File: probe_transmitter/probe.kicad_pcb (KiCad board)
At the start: 2 copper layers, 28.5 x 28.5 mm, 22 parts, among them J2 Conn_01x06, Q1 PMST2222, Q2 PMST2222, U2 ATtiny84-20M

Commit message: -add fix connector
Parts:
- added +1: PB0, TestPoint:TestPoint_Pad_D1.0mm, B.Cu at (109.6, 109.0)
- added -1: PB0, TestPoint:TestPoint_Pad_D1.0mm, B.Cu at (107.9, 110.6)
- R1: value R39 -> R1K
- R2: value R39 -> R1k
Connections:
- J2 pad 1: +3.3V -> GND
- J2 pad 6: GND -> +3.3V
- Q1 pad 3: Net-(J2-Pin_2) -> Net-(J2-Pin_5)
- Q2 pad 3: Net-(J2-Pin_3) -> Net-(J2-Pin_4)
- R5 pad 1: Net-(J2-Pin_2) -> Net-(J2-Pin_5)
- U2 pad 15: Net-(J2-Pin_5) -> Net-(J2-Pin_2)
- U2 pad 3: Net-(J2-Pin_4) -> Net-(J2-Pin_3)
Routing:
- net +3.3V: track 31.4 -> 61.0 mm
- net GND: track 28.8 -> 46.5 mm, vias 2 -> 1
- net Net-(J2-Pin_2): track 19.4 -> 36.3 mm, vias 1 -> 3
- net Net-(J2-Pin_4): track 19.5 -> 31.8 mm
- net Net-(J2-Pin_3): track 29.9 -> 20.3 mm
- net Net-(J2-Pin_5): track 24.5 -> 21.4 mm
- net /PAD1: track 69.8 -> 69.3 mm
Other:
- board text added: "G"

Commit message: -add to production
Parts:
- removed +1, -1, MOSI1: PB0, TestPoint:TestPoint_Pad_D1.0mm
- removed the ? at (111.3, 98.1)
- removed the ? at (111.3, 101.9)
- removed MISO1: PB1, TestPoint:TestPoint_Pad_D1.0mm
- removed RES1: PB5, TestPoint:TestPoint_Pad_D1.0mm
- removed SCL1: PB2, TestPoint:TestPoint_Pad_D1.0mm
- added +: PB0, TestPoint:TestPoint_Pad_D1.0mm, B.Cu at (105.1, 98.7)
- added -: PB0, TestPoint:TestPoint_Pad_D1.0mm, B.Cu at (104.7, 101.5)
- added ?: , , F.Cu at (110.3, 97.5)
- added ?: , , F.Cu at (110.3, 101.3)
- added MISO: PB1, TestPoint:TestPoint_Pad_D1.0mm, F.Cu at (106.9, 110.0)
- added MOSI: PB0, TestPoint:TestPoint_Pad_D1.0mm, F.Cu at (104.9, 111.2)
- added RES: PB5, TestPoint:TestPoint_Pad_D1.0mm, F.Cu at (102.8, 112.1)
- added SCL: PB2, TestPoint:TestPoint_Pad_D1.0mm, F.Cu at (108.6, 108.4)
-  : value Touch Probe v1.4 -> Touch Probe v1.5
- moved D4 1.61 mm to (99.0, 91.9)
- moved   1.17 mm to (90.0, 99.3)
- moved 1 1.17 mm to (91.7, 90.6)
- moved 2 1.17 mm to (94.9, 88.7)
- moved 3 1.17 mm to (95.0, 110.2)
- moved D5 1.17 mm to (98.9, 106.3)
- moved J2 1.17 mm to (102.8, 93.0)
- moved Q1 1.17 mm to (87.4, 97.4)
- moved Q2 1.17 mm to (87.4, 100.9)
- moved R1 1.17 mm to (90.1, 97.4)
- moved R2 1.17 mm to (90.1, 100.9)
- moved R5 1.17 mm to (91.7, 97.4)
- moved R6 1.17 mm to (91.7, 100.9)
- moved R7 1.17 mm to (92.3, 104.2)
- moved U2 1.17 mm to (103.8, 106.1)
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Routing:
- net +3.3V: track 61.0 -> 15.8 mm
- net Net-(J2-Pin_3): track 20.3 -> 21.5 mm
- net Net-(J2-Pin_5): track 21.4 -> 20.2 mm
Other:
- board text added: "+"
- board text added: "-"
- board text added: "LOW"
- board text added: "TOCH"
- board text removed: "G"

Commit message: -change hole ball 3.25/2.5
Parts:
-  : value Touch Probe v1.5 -> Touch Probe v1.6
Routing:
- net GND: track 46.3 -> 47.0 mm
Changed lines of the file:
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@@
 		(pad "1" thru_hole circle
 			(at 0 0)
-			(size 2.5 2.5)
-			(drill 1.6)
+			(size 3.25 3.25)
+			(drill 2.5)
 			(layers "*.Cu" "*.Mask")
 			(remove_unused_layers no)
@@
 		(pad "1" thru_hole circle
 			(at 0 0)
-			(size 2.5 2.5)
-			(drill 1.6)
+			(size 3.25 3.25)
+			(drill 2.5)
 			(layers "*.Cu" "*.Mask")
 			(remove_unused_layers no)
@@
 		(pad "1" thru_hole circle
 			(at 0 0)
-			(size 2.5 2.5)
-			(drill 1.6)
+			(size 3.25 3.25)
+			(drill 2.5)
 			(layers "*.Cu" "*.Mask")
 			(remove_unused_layers no)
@@
 		(pad "1" thru_hole circle
 			(at 0 0)
-			(size 2.5 2.5)
-			(drill 1.6)
+			(size 3.25 3.25)
+			(drill 2.5)
 			(layers "*.Cu" "*.Mask")
 			(remove_unused_layers no)
@@
 		(pad "1" thru_hole circle
 			(at 0 0 120)
-			(size 2.5 2.5)
-			(drill 1.6)
+			(size 3.25 3.25)
+			(drill 2.5)
 			(layers "*.Cu" "*.Mask")
 			(remove_unused_layers no)
@@
 		(pad "1" thru_hole circle
 			(at 0 0 240)
-			(size 2.5 2.5)
-			(drill 1.6)
+			(size 3.25 3.25)
+			(drill 2.5)
 			(layers "*.Cu" "*.Mask")
 			(remove_unused_layers no)
@@
 			)
 		)
-		(property "Value" "Touch Probe v1.5"
+		(property "Value" "Touch Probe v1.6"
 			(at -9.05 -7.21 0)
 			(layer "B.SilkS")
@@
 		)
 	)
+	(dimension
+		(type radial)
+		(layer "F.SilkS")
+		(pts
+			(xy 94.921869 88.680014) (xy 91.654633 90.600995)
+		)
+		(leader_length 3.81)
+		(format
+			(prefix "R ")
+			(suffix "")
+			(units 3)
+			(units_format 1)
+			(precision 4)
+		)
+		(style
+			(thickness 0.15)
+			(arrow_length 1.27)
+			(text_position_mode 0)
+			(extension_offset 0.5)
+			(keep_text_aligned yes)
+		)
+		(gr_text "R 3.7901 mm"
+			(at 75.670258 92.532053 0)
+			(layer "F.SilkS")
+			(effects
+				(font
+					(size 1 1)
+					(thickness 0.15)
+				)
+			)
+		)
+	)
 	(segment
 		(start 101.715693 104.719545)
@@
 	)
 	(segment
-		(start 86.412953 101.51205)
-		(end 86.412915 101.879564)
+		(start 101.972794 104.269559)
+		(end 102.413328 104.710089)
 		(width 0.25)
 		(layer "F.Cu")
@@
 	)
 	(segment
-		(start 85.360419 100.459563)
-		(end 85.35494 100.336376)
+		(start 85.349435 100.3231)
+		(end 85.349453 100.330871)
 		(width 0.25)
 		(layer "F.Cu")
@@
 	)
 	(segment
-		(start 101.972794 104.269559)
-		(end 102.413328 104.710089)
+		(start 86.412953 101.51205)
+		(end 86.412915 101.879564)
 		(width 0.25)
 		(layer "F.Cu")
@@
 	)
 	(segment
-		(start 85.349435 100.3231)
-		(end 85.349453 100.330871)
+		(start 85.360436 98.709557)
+		(end 85.670435 98.399556)
 		(width 0.25)
 		(layer "F.Cu")
@@
 	)
 	(segment
-		(start 91.114049 110.173165)
-		(end 89.770435 108.829556)
+		(start 85.360435 99.617234)
+		(end 85.349429 99.628233)
 		(width 0.25)
 		(layer "F.Cu")
@@
 	)
 	(segment
-		(start 87.430415 105.679565)
-		(end 89.770422 108.019562)
+		(start 94.499406 110.68)
+		(end 95.006237 110.173169)
 		(width 0.25)
 		(layer "F.Cu")
@@
 	)
 	(segment
-		(start 86.412915 101.879564)
-		(end 87.430434 102.897057)
+		(start 100.960439 104.269566)
+		(end 101.972794 104.269559)
 		(width 0.25)
 		(layer "F.Cu")
@@
 	)
 	(segment
-		(start 85.360436 98.709557)
-		(end 85.670435 98.399556)
+		(start 89.51 109)
+		(end 91.19 110.68)
 		(width 0.25)
 		(layer "F.Cu")
@@
 	)
 	(segment
-		(start 85.360435 99.617234)
-		(end 85.349429 99.628233)
+		(start 87.430415 105.679565)
+		(end 89.51 107.75915)
 		(width 0.25)
 		(layer "F.Cu")
@@
 	)
 	(segment
-		(start 100.960439 104.269566)
-		(end 101.972794 104.269559)
+		(start 85.349435 100.3231)
+		(end 85.349435 99.636013)
 		(width 0.25)
 		(layer "F.Cu")
@@
 	)
 	(segment
-		(start 85.349435 100.3231)
-		(end 85.349435 99.636013)
+		(start 85.670435 98.399556)
+		(end 86.412935 98.399557)
 		(width 0.25)
 		(layer "F.Cu")
@@
 	)
 	(segment
-		(start 85.670435 98.399556)
-		(end 86.412935 98.399557)
+		(start 85.360419 100.459563)
+		(end 86.412953 101.51205)
 		(width 0.25)
 		(layer "F.Cu")
@@
 	)
 	(segment
-		(start 89.770435 108.829556)
-		(end 89.770422 108.019562)
+		(start 85.35494 100.336376)
+		(end 85.360419 100.459563)
 		(width 0.25)
 		(layer "F.Cu")
@@
 	)
 	(segment
-		(start 86.412953 101.51205)
-		(end 85.360419 100.459563)
+		(start 91.19 110.68)
+		(end 94.499406 110.68)
 		(width 0.25)
 		(layer "F.Cu")
@@
 	)
 	(segment
-		(start 85.354935 100.336379)
-		(end 85.349453 100.330871)
+		(start 89.51 107.75915)
+		(end 89.51 109)
 		(width 0.25)
 		(layer "F.Cu")
@@
 	)
 	(segment
-		(start 91.114049 110.173165)
-		(end 95.006237 110.173169)
+		(start 85.354935 100.336379)
+		(end 85.349453 100.330871)
 		(width 0.25)
 		(layer "F.Cu")
@@
 		(width 0.25)
 		(layer "F.Cu")
+		(net 2)
+	)
+	(segment
+		(start 86.412915 101.879564)
+		(end 87.430434 102.897057)
+		(width 0.25)
+		(layer "F.Cu")

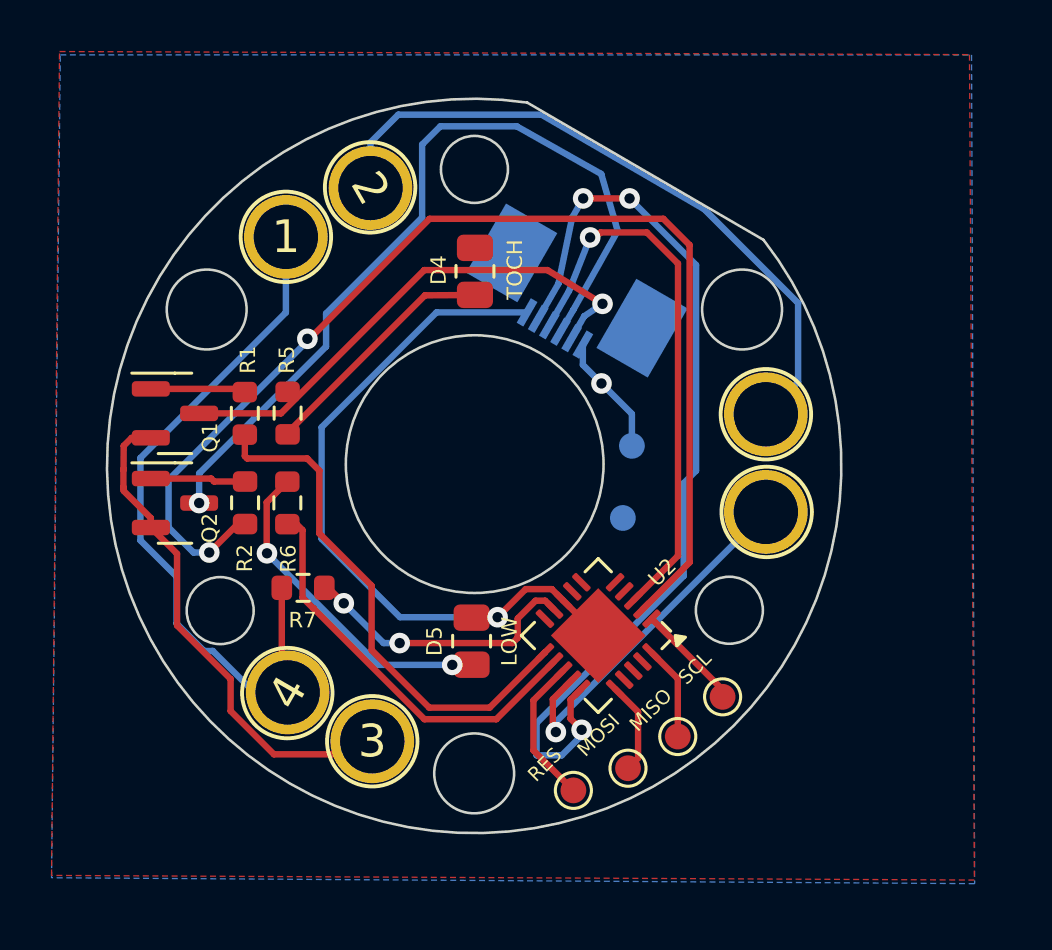
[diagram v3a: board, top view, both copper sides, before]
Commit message: -add 4.54mm ball distance
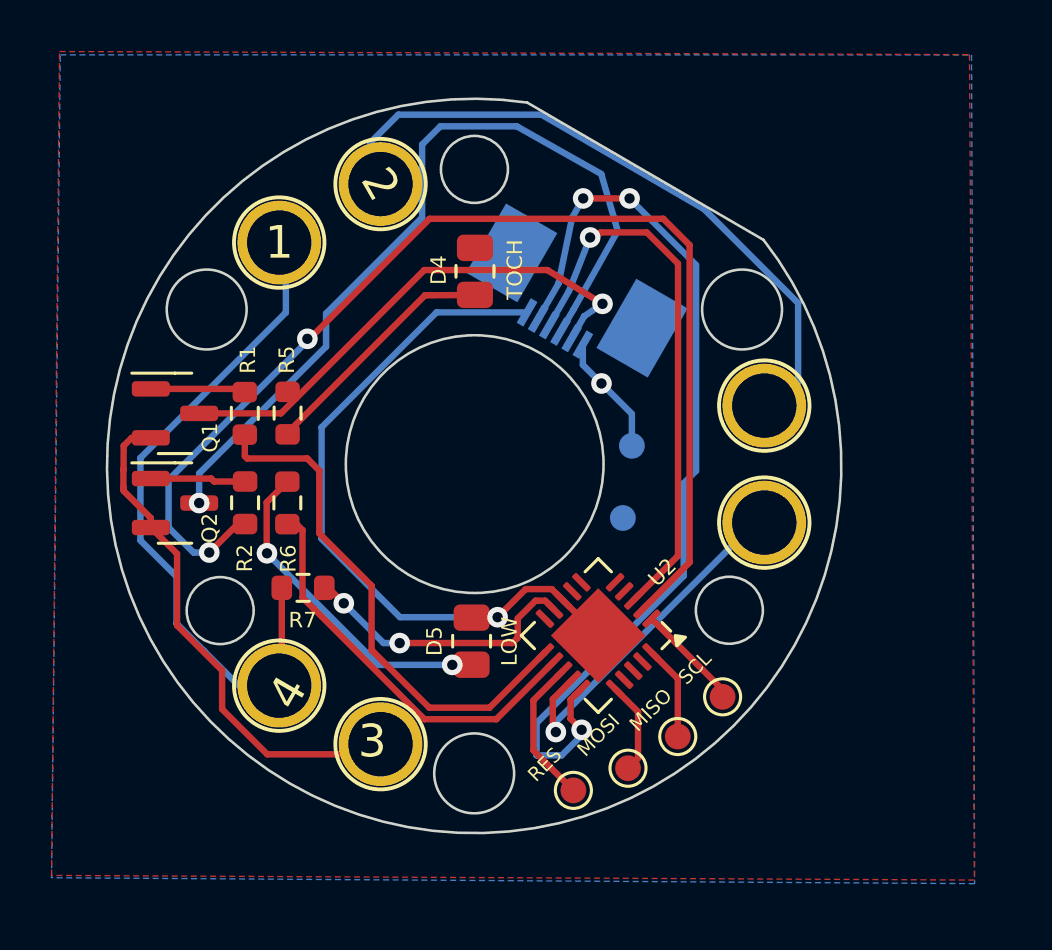
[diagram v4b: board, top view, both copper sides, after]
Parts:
- moved 2 0.42 mm to (95.3, 88.6)
- moved 1 0.34 mm to (91.4, 90.8)
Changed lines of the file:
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@@
 		)
 		(pad "1" thru_hole circle
-			(at 0 0)
+			(at -0.062495 -0.334947)
 			(size 3.25 3.25)
 			(drill 2.5)
@@
 	(footprint ""
 		(layer "F.Cu")
-		(at 91.654633 90.600995)
+		(at 91.39581 90.82259)
 		(property "Reference" "1"
 			(at 0 0 0)
@@
 		)
 		(pad "1" thru_hole circle
-			(at 0 0)
+			(at -0.062495 0.415053)
 			(size 3.25 3.25)
 			(drill 2.5)
@@
 		)
 		(pad "1" thru_hole circle
-			(at 0 0)
+			(at 0.321323 0.113351)
 			(size 3.25 3.25)
 			(drill 2.5)
@@
 	(footprint ""
 		(layer "F.Cu")
-		(at 94.936869 88.705995 120)
+		(at 95.32756 88.55259 120)
 		(property "Reference" "2"
 			(at 0 0 120)
@@
 		)
 		(pad "1" thru_hole circle
-			(at 0 0 240)
+			(at -0.062499 0.415046 240)
 			(size 3.25 3.25)
 			(drill 2.5)
@@
 	)
 	(gr_circle
-		(center 95.006237 110.173169)
-		(end 96.761287 110.173169)
+		(center 95.32756 110.28652)
+		(end 97.08261 110.28652)
 		(stroke
 			(width 0.15)
@@
 	)
 	(gr_circle
-		(center 94.921869 88.680014)
-		(end 96.676919 88.680014)
+		(center 95.32756 88.55259)
+		(end 97.08261 88.55259)
 		(stroke
 			(width 0.15)
@@
 	)
 	(gr_circle
-		(center 110.310435 101.274507)
-		(end 112.065485 101.274507)
+		(center 110.21794 101.68956)
+		(end 111.97299 101.68956)
 		(stroke
 			(width 0.15)
@@
 	)
 	(gr_circle
-		(center 91.654633 90.600995)
-		(end 93.409683 90.600995)
+		(center 91.39581 90.82259)
+		(end 93.15086 90.82259)
 		(stroke
 			(width 0.15)
@@
 	)
 	(gr_circle
-		(center 91.709001 108.30415)
-		(end 93.464051 108.30415)
+		(center 91.39581 108.01652)
+		(end 93.15086 108.01652)
 		(stroke
 			(width 0.15)
@@
 	)
 	(gr_circle
-		(center 110.280435 97.484507)
-		(end 112.035485 97.484507)
+		(center 110.21794 97.14956)
+		(end 111.97299 97.14956)
 		(stroke
 			(width 0.15)
@@
 		)
 	)
-	(dimension
-		(type radial)
-		(layer "F.SilkS")
-		(pts
-			(xy 94.921869 88.680014) (xy 91.654633 90.600995)
-		)
-		(leader_length 3.81)
-		(format
-			(prefix "R ")
-			(suffix "")
-			(units 3)
-			(units_format 1)
-			(precision 4)
-		)
-		(style
-			(thickness 0.15)
-			(arrow_length 1.27)
-			(text_position_mode 0)
-			(extension_offset 0.5)
-			(keep_text_aligned yes)
-		)
-		(gr_text "R 3.7901 mm"
-			(at 75.670258 92.532053 0)
-			(layer "F.SilkS")
-			(effects
-				(font
-					(size 1 1)
-					(thickness 0.15)
-				)
-			)
-		)
-	)
 	(segment
 		(start 101.715693 104.719545)
@@
 	)
 	(segment
+		(start 85.35494 100.336376)
+		(end 85.360419 100.459563)
+		(width 0.25)
+		(layer "F.Cu")
+		(net 2)
+	)
+	(segment
 		(start 102.413328 104.710089)
 		(end 103.774509 106.07127)
@@
 	)
 	(segment
-		(start 85.349435 100.3231)
-		(end 85.349453 100.330871)
+		(start 87.430415 105.679565)
+		(end 89.18 107.42915)
 		(width 0.25)
 		(layer "F.Cu")
@@
 	)
 	(segment
-		(start 86.412953 101.51205)
-		(end 86.412915 101.879564)
+		(start 85.349435 100.3231)
+		(end 85.349453 100.330871)
 		(width 0.25)
 		(layer "F.Cu")
@@
 	)
 	(segment
-		(start 85.360436 98.709557)
-		(end 85.670435 98.399556)
+		(start 89.18 108.93)
+		(end 90.93 110.68)
 		(width 0.25)
 		(layer "F.Cu")
@@
 	)
 	(segment
-		(start 85.360435 99.617234)
-		(end 85.349429 99.628233)
+		(start 89.18 107.42915)
+		(end 89.18 108.93)
 		(width 0.25)
 		(layer "F.Cu")
@@
 	)
 	(segment
-		(start 94.499406 110.68)
-		(end 95.006237 110.173169)
+		(start 85.360436 98.709557)
+		(end 85.670435 98.399556)
 		(width 0.25)
 		(layer "F.Cu")
@@
 	)
 	(segment
-		(start 100.960439 104.269566)
-		(end 101.972794 104.269559)
+		(start 85.360435 99.617234)
+		(end 85.349429 99.628233)
 		(width 0.25)
 		(layer "F.Cu")
@@
 	)
 	(segment
-		(start 89.51 109)
-		(end 91.19 110.68)
+		(start 86.412953 101.51205)
+		(end 86.412915 101.879564)
 		(width 0.25)
 		(layer "F.Cu")
@@
 	)
 	(segment
-		(start 87.430415 105.679565)
-		(end 89.51 107.75915)
+		(start 100.960439 104.269566)
+		(end 101.972794 104.269559)
 		(width 0.25)
 		(layer "F.Cu")
@@
 	)
 	(segment
-		(start 85.670435 98.399556)
-		(end 86.412935 98.399557)
+		(start 90.93 110.68)
+		(end 94.499406 110.68)
 		(width 0.25)
 		(layer "F.Cu")
@@
 	)
 	(segment
-		(start 85.360419 100.459563)
-		(end 86.412953 101.51205)
+		(start 85.670435 98.399556)
+		(end 86.412935 98.399557)
 		(width 0.25)
 		(layer "F.Cu")
@@
 	)
 	(segment
-		(start 85.35494 100.336376)
-		(end 85.360419 100.459563)
-		(width 0.25)
-		(layer "F.Cu")
-		(net 2)
-	)
-	(segment
-		(start 91.19 110.68)
-		(end 94.499406 110.68)
+		(start 85.360419 100.459563)
+		(end 86.412953 101.51205)
 		(width 0.25)
 		(layer "F.Cu")
@@
 	)
 	(segment
-		(start 89.51 107.75915)
-		(end 89.51 109)
+		(start 87.430434 102.897057)
+		(end 87.430415 105.679565)
 		(width 0.25)
 		(layer "F.Cu")
@@
 	)
 	(segment
-		(start 87.430434 102.897057)
-		(end 87.430415 105.679565)
+		(start 86.412915 101.879564)
+		(end 87.430434 102.897057)
 		(width 0.25)
 		(layer "F.Cu")
@@
 	)
 	(segment
-		(start 86.412915 101.879564)
-		(end 87.430434 102.897057)
+		(start 94.499406 110.68)
+		(end 95.006237 110.173169)
 		(width 0.25)
 		(layer "F.Cu")
@@
 	)
 	(segment
-		(start 88.480433 106.669561)
-		(end 87.410433 105.599557)
+		(start 102.129653 109.425278)
+		(end 110.280435 101.274507)
 		(width 0.25)
 		(layer "B.Cu")
@@
 	)
 	(segment
-		(start 90.429041 108.278182)
-		(end 91.724001 108.278169)
+		(start 86.010456 102.379548)
+		(end 87.410445 103.779553)
 		(width 0.25)
 		(layer "B.Cu")
@@
 	)
 	(segment
-		(start 102.129653 109.425278)
-		(end 110.280435 101.274507)
+		(start 87.410433 105.599557)
+		(end 88.480433 106.669561)
 		(width 0.25)
 		(layer "B.Cu")
@@
 	)
 	(segment
-		(start 88.820436 106.669553)
-		(end 90.429041 108.278182)
+		(start 86.010423 99.179552)
+		(end 86.010456 102.379548)
 		(width 0.25)
 		(layer "B.Cu")
@@
 	)
 	(segment
-		(start 88.820436 106.669553)
-		(end 88.480433 106.669561)
+		(start 88.480437 106.669561)
+		(end 90.089045 108.278169)
 		(width 0.25)
 		(layer "B.Cu")
@@
 	)
 	(segment
-		(start 94.93686 86.938225)
-		(end 96.015534 85.85954)
+		(start 91.654624 93.535355)
+		(end 86.010423 99.179552)
 		(width 0.25)
 		(layer "B.Cu")
@@
 	)
 	(segment
-		(start 86.010423 99.179552)
-		(end 91.654624 93.535355)
+		(start 88.480433 106.669561)
+		(end 88.480437 106.669561)
 		(width 0.25)
 		(layer "B.Cu")
@@
 	)
 	(segment
-		(start 87.410433 105.599557)
-		(end 87.410445 103.779553)
+		(start 94.93686 86.938225)
+		(end 96.015534 85.85954)
 		(width 0.25)
 		(layer "B.Cu")
@@
 	)
 	(segment
-		(start 96.015534 85.85954)
-		(end 101.575627 85.859564)
+		(start 91.654633 90.600995)
+		(end 91.654624 93.535355)
 		(width 0.25)
 		(layer "B.Cu")
@@
 	)
 	(segment
-		(start 111.530448 93.16955)
-		(end 111.530447 96.234513)
+		(start 96.015534 85.85954)
+		(end 101.575627 85.859564)
 		(width 0.25)
 		(layer "B.Cu")
@@
 	)
 	(segment
-		(start 86.010456 102.379548)
-		(end 86.010423 99.179552)
+		(start 90.089045 108.278169)
+		(end 91.724001 108.278169)
 		(width 0.25)
 		(layer "B.Cu")
@@
 	)
 	(segment
-		(start 102.129653 109.425278)
-		(end 102.129661 109.816347)
+		(start 111.530448 93.16955)
+		(end 111.530447 96.234513)
 		(width 0.25)
 		(layer "B.Cu")
@@
 	)
 	(segment
-		(start 91.654624 93.535355)
-		(end 91.654633 90.600995)
+		(start 102.129653 109.425278)
+		(end 102.129661 109.816347)
 		(width 0.25)
 		(layer "B.Cu")
@@
 	)
 	(segment
-		(start 86.010456 102.379548)
-		(end 87.410445 103.779553)
+		(start 111.530448 93.16955)
+		(end 107.888733 89.527857)
 		(width 0.25)
 		(layer "B.Cu")
@@
 	)
 	(segment
-		(start 111.530448 93.16955)
-		(end 107.888733 89.527857)
+		(start 87.410445 103.779553)
+		(end 87.410433 105.599557)
 		(width 0.25)
 		(layer "B.Cu")
